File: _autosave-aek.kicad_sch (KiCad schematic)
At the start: 239 parts, among them J1 Conn_01x04_MountingPin, SW1 SW_Push, U1 ATmega32U4-AU, Y1 16MHz

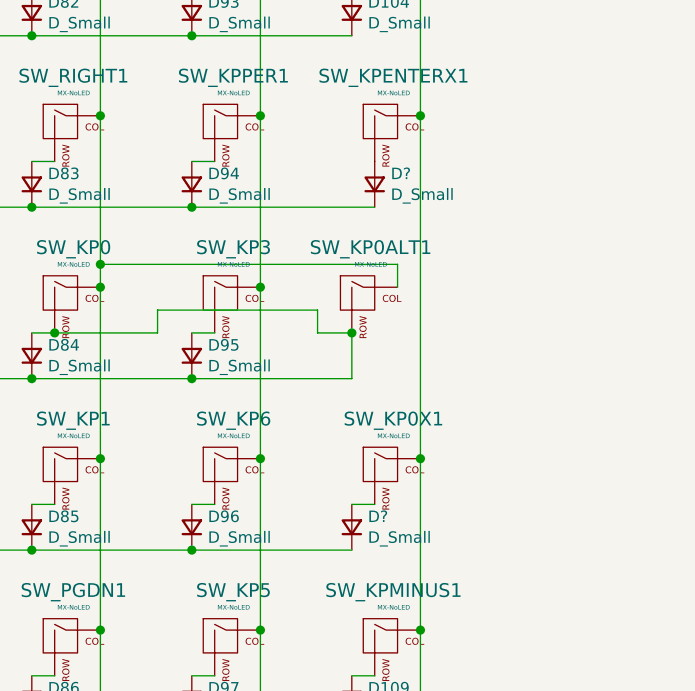
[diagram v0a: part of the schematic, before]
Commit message: grid option on numpad
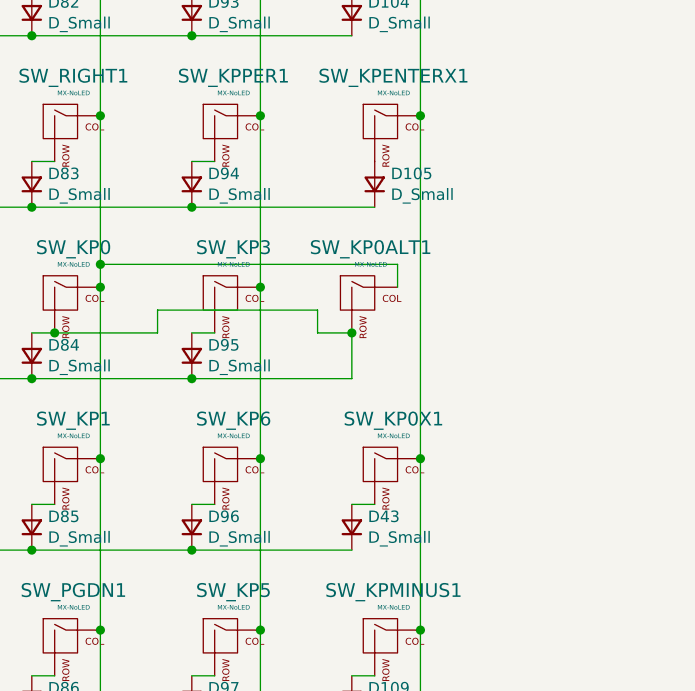
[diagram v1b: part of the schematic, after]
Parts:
- SW_KP0ALT1, SW_KPENTERALT1, SW_KPENTERX1: footprint MX_Alps_Hybrid:MX-2U-ReversedStabilizers-NoLED -> MX_Alps_Hybrid:MX-1U-NoLED
- gave numbers to parts that had none: 2
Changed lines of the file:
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@@
   (symbol (lib_id "Device:D_Small") (at 314.96 186.69 90) (unit 1)
     (in_bom yes) (on_board yes)
-    (property "Reference" "D?" (id 0) (at 316.738 185.5216 90)
+    (property "Reference" "D43" (id 0) (at 316.738 185.5216 90)
       (effects (font (size 1.27 1.27)) (justify right))
     )
@@
   (symbol (lib_id "Device:D_Small") (at 317.5 148.59 90) (unit 1)
     (in_bom yes) (on_board yes)
-    (property "Reference" "D?" (id 0) (at 319.278 147.4216 90)
+    (property "Reference" "D105" (id 0) (at 319.278 147.4216 90)
       (effects (font (size 1.27 1.27)) (justify right))
     )
@@
       (effects (font (size 0.508 0.508)))
     )
-    (property "Footprint" "MX_Alps_Hybrid:MX-2U-ReversedStabilizers-NoLED" (id 2) (at 300.355 161.925 0)
+    (property "Footprint" "MX_Alps_Hybrid:MX-1U-NoLED" (id 2) (at 300.355 161.925 0)
       (effects (font (size 1.524 1.524)) hide)
     )
@@
       (effects (font (size 0.508 0.508)))
     )
-    (property "Footprint" "MX_Alps_Hybrid:MX-2U-ReversedStabilizers-NoLED" (id 2) (at 302.895 142.875 0)
+    (property "Footprint" "MX_Alps_Hybrid:MX-1U-NoLED" (id 2) (at 302.895 142.875 0)
       (effects (font (size 1.524 1.524)) hide)
     )
@@
       (effects (font (size 0.508 0.508)))
     )
-    (property "Footprint" "MX_Alps_Hybrid:MX-2U-ReversedStabilizers-NoLED" (id 2) (at 323.215 123.825 0)
+    (property "Footprint" "MX_Alps_Hybrid:MX-1U-NoLED" (id 2) (at 323.215 123.825 0)
       (effects (font (size 1.524 1.524)) hide)
     )
@@
       (reference "D42") (unit 1) (value "D_Small") (footprint "Diode_SMD:D_SOD-123")
     )
+    (path "/0a9f023d-4fb2-47e0-ae5e-92c3e1654ff1"
+      (reference "D43") (unit 1) (value "D_Small") (footprint "Diode_SMD:D_SOD-123")
+    )
     (path "/00000000-0000-0000-0000-00006145a3a3"
       (reference "D44") (unit 1) (value "D_Small") (footprint "Diode_SMD:D_SOD-123")
@@
       (reference "D104") (unit 1) (value "D_Small") (footprint "Diode_SMD:D_SOD-123")
     )
+    (path "/d2e42852-7fb4-474f-a864-b3c20a8b77a0"
+      (reference "D105") (unit 1) (value "D_Small") (footprint "Diode_SMD:D_SOD-123")
+    )
     (path "/00000000-0000-0000-0000-00006145a285"
       (reference "D109") (unit 1) (value "D_Small") (footprint "Diode_SMD:D_SOD-123")
@@
       (reference "D110") (unit 1) (value "D_Small") (footprint "Diode_SMD:D_SOD-123")
     )
-    (path "/0a9f023d-4fb2-47e0-ae5e-92c3e1654ff1"
-      (reference "D?") (unit 1) (value "D_Small") (footprint "Diode_SMD:D_SOD-123")
-    )
-    (path "/d2e42852-7fb4-474f-a864-b3c20a8b77a0"
-      (reference "D?") (unit 1) (value "D_Small") (footprint "Diode_SMD:D_SOD-123")
-    )
     (path "/00000000-0000-0000-0000-000061db0c88"
       (reference "H1") (unit 1) (value "MountingHole_Pad") (footprint "MountingHole:MountingHole_2.7mm_M2.5_Pad")
@@
     )
     (path "/764d3922-6c3b-4ad1-99f1-13051e884ac2"
-      (reference "SW_KP0ALT1") (unit 1) (value "MX-NoLED") (footprint "MX_Alps_Hybrid:MX-2U-ReversedStabilizers-NoLED")
+      (reference "SW_KP0ALT1") (unit 1) (value "MX-NoLED") (footprint "MX_Alps_Hybrid:MX-1U-NoLED")
     )
     (path "/204e0ee4-dec0-4dc2-b622-9ea13958f955"
@@
     )
     (path "/4f0dc72b-fb67-4861-96c0-74fd1311c468"
-      (reference "SW_KPENTERALT1") (unit 1) (value "MX-NoLED") (footprint "MX_Alps_Hybrid:MX-2U-ReversedStabilizers-NoLED")
+      (reference "SW_KPENTERALT1") (unit 1) (value "MX-NoLED") (footprint "MX_Alps_Hybrid:MX-1U-NoLED")
     )
     (path "/045dc86d-b269-41b1-9424-1a177a9b131f"
-      (reference "SW_KPENTERX1") (unit 1) (value "MX-NoLED") (footprint "MX_Alps_Hybrid:MX-2U-ReversedStabilizers-NoLED")
+      (reference "SW_KPENTERX1") (unit 1) (value "MX-NoLED") (footprint "MX_Alps_Hybrid:MX-1U-NoLED")
     )
     (path "/00000000-0000-0000-0000-00006145a32b"
